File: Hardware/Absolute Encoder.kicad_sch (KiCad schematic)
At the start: 13 parts, among them J1 PISO_OUT, J2 PISO_IN, U1 74LS165

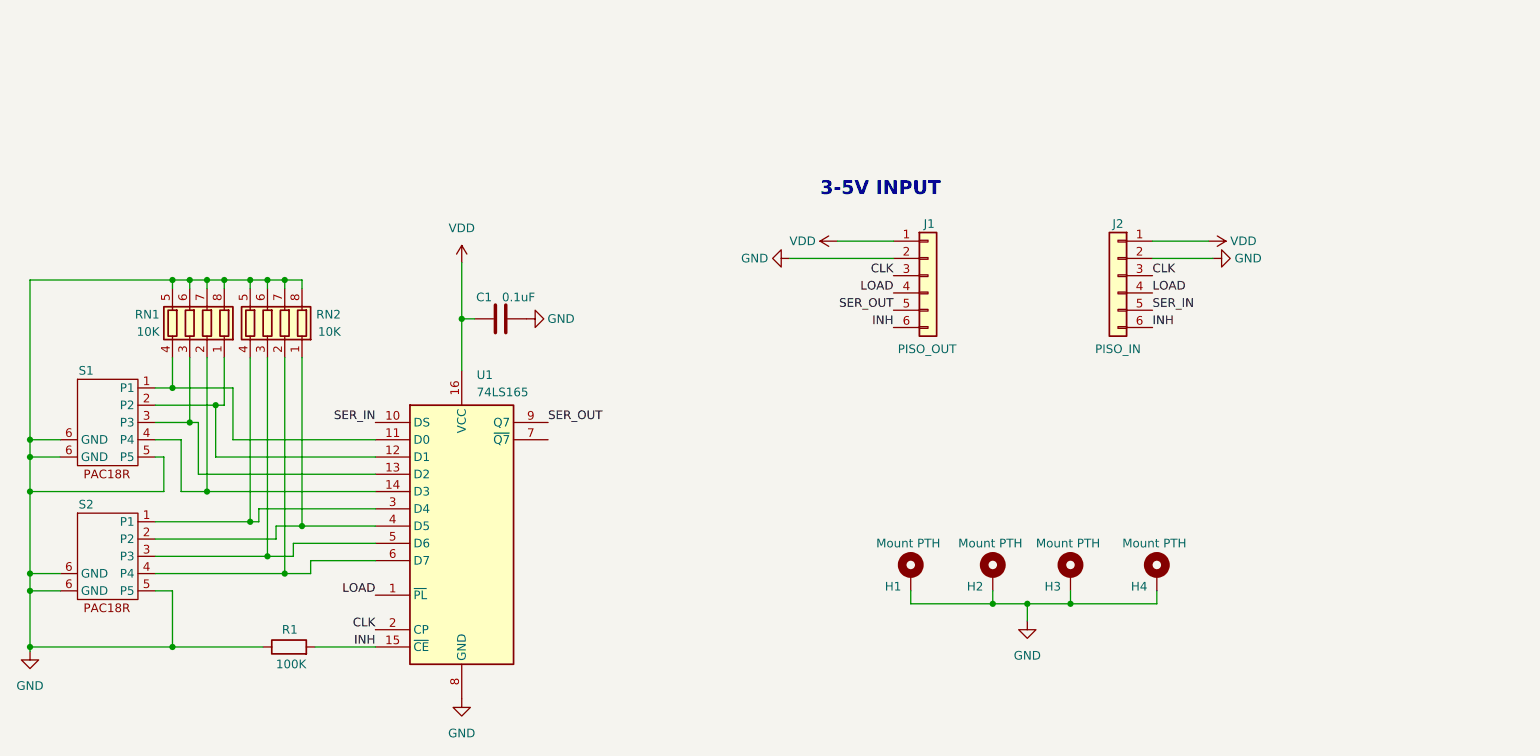
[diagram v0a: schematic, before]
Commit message: change R network for individual Rs
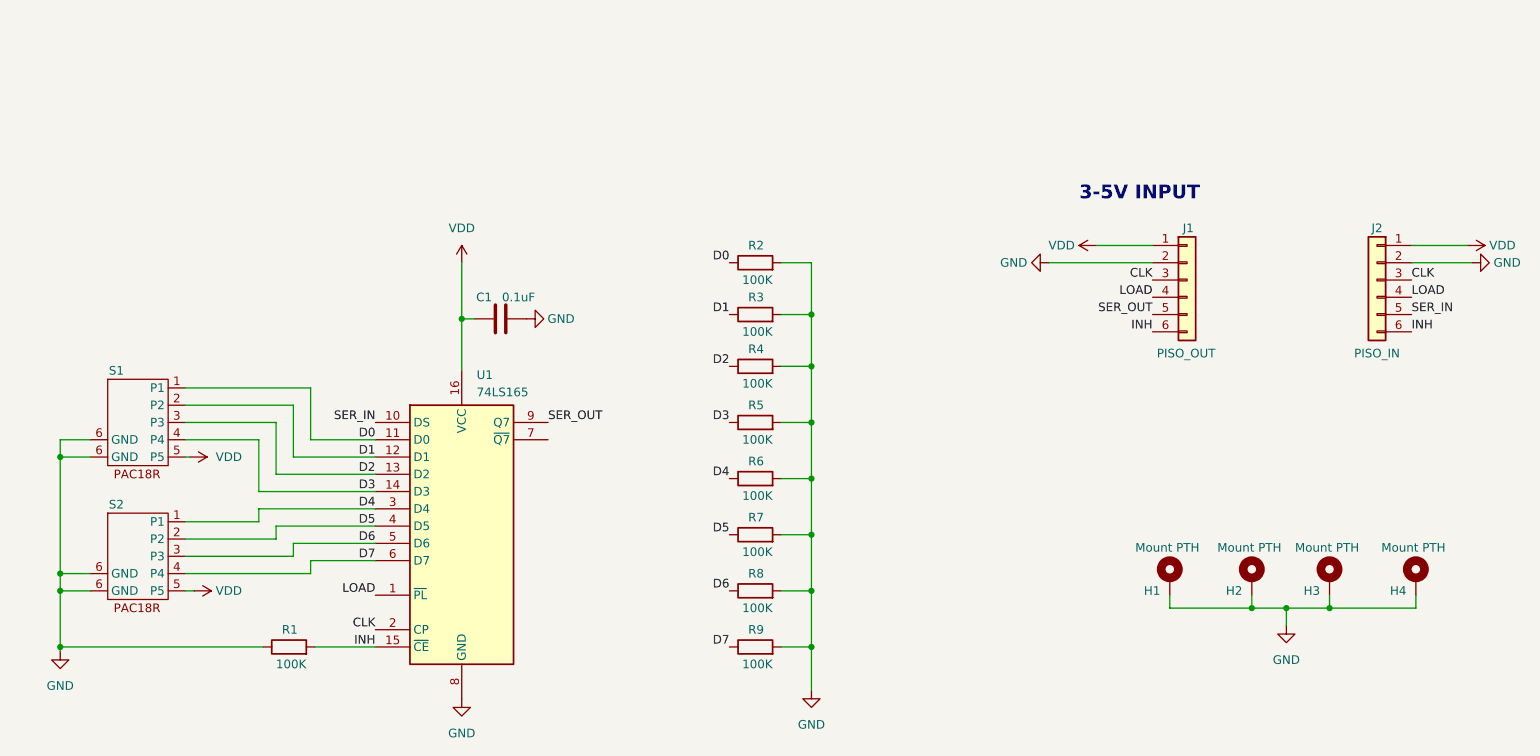
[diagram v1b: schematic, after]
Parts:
- removed RN1, RN2: 10K, Resistor_SMD:R_Array_Concave_4x0402, symbol Device:R_Pack04
- added R2, R3, R4, R5, R6, R7, R8, R9: 100K, Resistor_SMD:R_0402_1005Metric, symbol Device:R
- R1: footprint Resistor_SMD:R_0603_1608Metric -> Resistor_SMD:R_0402_1005Metric
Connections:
- net GND: now also R2.2, R3.2, R4.2, R5.2, R6.2, R7.2, R8.2, R9.2; no longer S1.5 (P5), S2.5 (P5)
- net VDD: now also S1.5 (P5), S2.5 (P5)
- net D4: now reaches S2.1 (P1), U1.3 (D4)
- net D4: now also R6.1
- net D5: now reaches S2.2 (P2), U1.4 (D5)
- net D5: now also R7.1
- net D6: now reaches S2.3 (P3), U1.5 (D6)
- net D6: now also R8.1
- net D7: now reaches S2.4 (P4), U1.6 (D7)
- net D7: now also R9.1
- net D0: now reaches S1.1 (P1), U1.11 (D0)
- net D0: now also R2.1
- net D1: now reaches S1.2 (P2), U1.12 (D1)
- net D1: now also R3.1
- net D2: now reaches S1.3 (P3), U1.13 (D2)
- net D2: now also R4.1
- net D3: now reaches S1.4 (P4), U1.14 (D3)
- net D3: now also R5.1
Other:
- moved on the sheet: H1, H2, H3, H4, J1, J2, S1, S2

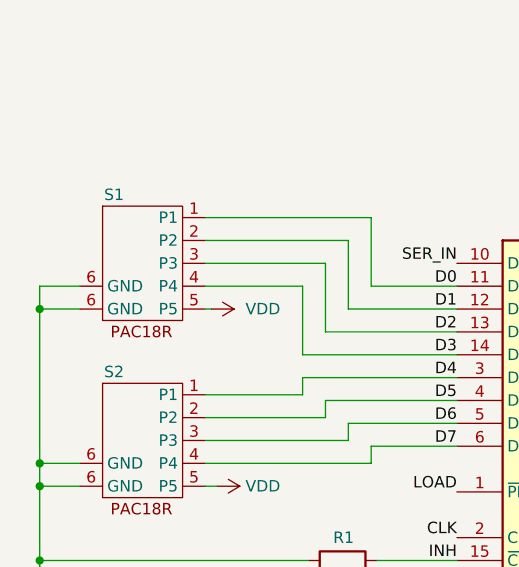
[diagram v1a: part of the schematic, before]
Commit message: Update Readme
add license
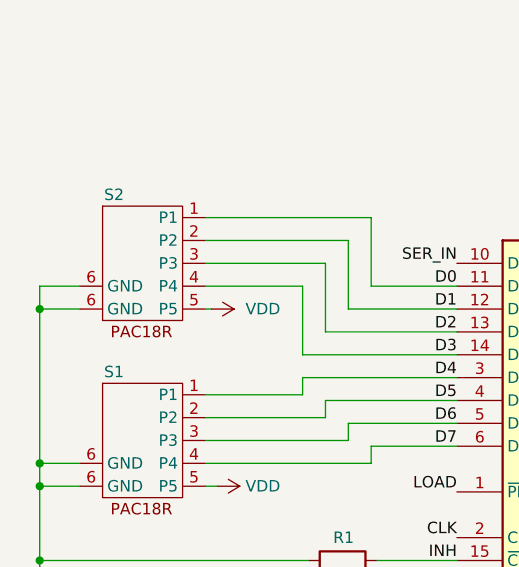
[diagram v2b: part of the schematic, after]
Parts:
- renumbered S2 to S1, S1 to S2
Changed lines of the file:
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@@
 		(on_board yes)
 		(dnp no)
-		(property "Reference" "S2"
+		(property "Reference" "S1"
 			(at 61.595 102.235 0)
 			(effects
@@
 			(project "Absolute Encoder"
 				(path "/e9a1f795-9b0b-4ff9-9b00-3d3b4875d365"
-					(reference "S2")
+					(reference "S1")
 					(unit 1)
 				)
@@
 		(on_board yes)
 		(dnp no)
-		(property "Reference" "S1"
+		(property "Reference" "S2"
 			(at 61.595 82.55 0)
 			(effects
@@
 			(project "Absolute Encoder"
 				(path "/e9a1f795-9b0b-4ff9-9b00-3d3b4875d365"
-					(reference "S1")
-					(unit 1)
-				)
+					(reference "S2")
+					(unit 1)
+				)

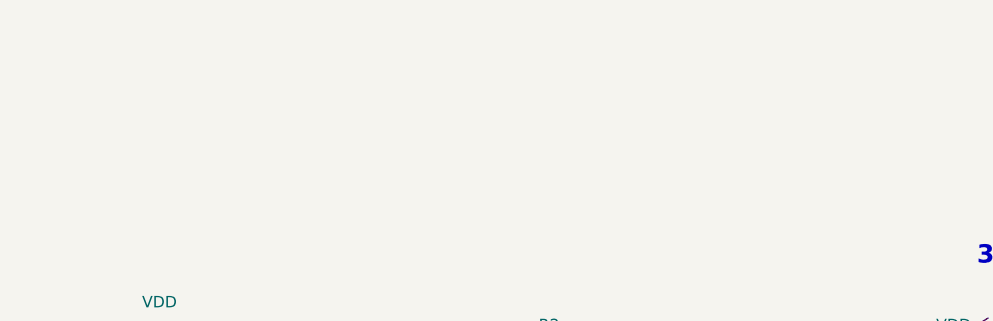
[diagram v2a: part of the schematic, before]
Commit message: Moved custom parts to local path
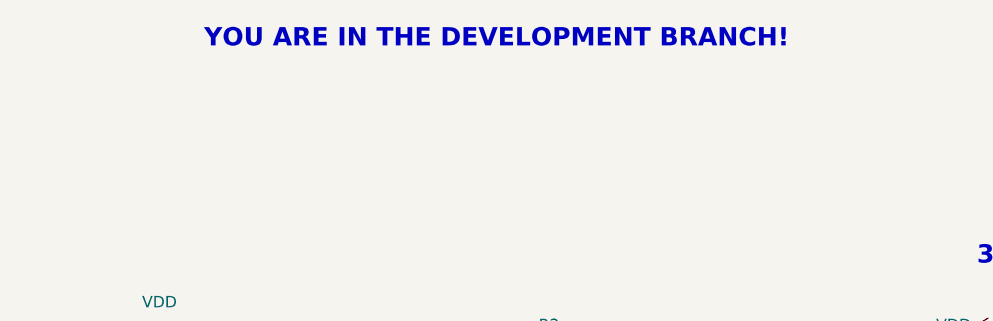
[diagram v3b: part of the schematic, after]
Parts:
- removed S1, S2: ~, Flywheel:PAC18R, symbol Flywheel_Library:PAC18R
- added S1, S2: ~, AbsoluteEncoder:PAC18R, symbol AbsoluteEncoder_Library:PAC18R
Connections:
- net D0: now also S2.1 (P1)
- net D1: now also S2.2 (P2)
- net D2: now also S2.3 (P3)
- net D3: now also S2.4 (P4)
- net D4: now also S1.1 (P1)
- net D5: now also S1.2 (P2)
- net D6: now also S1.3 (P3)
- net D7: now also S1.4 (P4)
- net GND: now also S1.6 (GND), S2.6 (GND)
- net VDD: now also S1.5 (P5), S2.5 (P5)
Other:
- note added: "YOU ARE IN THE DEVELOPMENT BRANCH!"
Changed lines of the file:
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@@
 		)
 	)
-	(text "3-5V INPUT"
-		(exclude_from_sim no)
-		(at 212.09 56.515 0)
+	(text "YOU ARE IN THE DEVELOPMENT BRANCH!"
+		(exclude_from_sim no)
+		(at 149.86 32.385 0)
 		(effects
 			(font
@@
 		)
 	)
+	(text "3-5V INPUT"
+		(exclude_from_sim no)
+		(at 212.09 56.515 0)
+		(effects
+			(font
+				(size 2.032 2.032)
+				(thickness 0.4064)
+				(bold yes)
+			)
+		)
+	)
 	(label "CLK"
 		(at 213.995 69.215 180)
@@
 				(path "/e9a1f795-9b0b-4ff9-9b00-3d3b4875d365"
 					(reference "#PWR09")
-					(unit 1)
-				)
-			)
-		)
-	)
-	(symbol
-		(lib_name "Flywheel_Library:PAC18R")
-		(lib_id "Flywheel_Library:PAC18R")
-		(at 64.135 109.855 0)
-		(unit 1)
-		(exclude_from_sim no)
-		(in_bom yes)
-		(on_board yes)
-		(dnp no)
-		(property "Reference" "S1"
-			(at 61.595 102.235 0)
-			(effects
-				(font
-					(size 1.27 1.27)
-				)
-			)
-		)
-		(property "Value" "~"
-			(at 64.77 102.235 0)
-			(effects
-				(font
-					(size 1.27 1.27)
-				)
-			)
-		)
-		(property "Footprint" "Flywheel:PAC18R"
-			(at 69.215 104.775 0)
-			(effects
-				(font
-					(size 1.27 1.27)
-				)
-				(hide yes)
-			)
-		)
-		(property "Datasheet" "https://www.mouser.com/datasheet/2/54/pac18r-2511013.pdf"
-			(at 69.215 104.775 0)
-			(effects
-				(font
-					(size 1.27 1.27)
-				)
-				(hide yes)
-			)
-		)
-		(property "Description" "Grey Code Encoder Switch"
-			(at 69.215 104.775 0)
-			(effects
-				(font
-					(size 1.27 1.27)
-				)
-				(hide yes)
-			)
-		)
-		(pin "3"
-		)
-		(pin "4"
-		)
-		(pin "5"
-		)
-		(pin "2"
-		)
-		(pin "1"
-		)
-		(pin "6"
-		)
-		(pin "6"
-		)
-		(instances
-			(project "Absolute Encoder"
-				(path "/e9a1f795-9b0b-4ff9-9b00-3d3b4875d365"
-					(reference "S1")
 					(unit 1)
 				)
@@
 	)
 	(symbol
+		(lib_name "AbsoluteEncoder_Library:PAC18R")
+		(lib_id "AbsoluteEncoder_Library:PAC18R")
+		(at 64.135 109.855 0)
+		(unit 1)
+		(exclude_from_sim no)
+		(in_bom yes)
+		(on_board yes)
+		(dnp no)
+		(property "Reference" "S1"
+			(at 61.595 102.235 0)
+			(effects
+				(font
+					(size 1.27 1.27)
+				)
+			)
+		)
+		(property "Value" "~"
+			(at 64.77 102.235 0)
+			(effects
+				(font
+					(size 1.27 1.27)
+				)
+			)
+		)
+		(property "Footprint" "AbsoluteEncoder:PAC18R"
+			(at 69.215 104.775 0)
+			(effects
+				(font
+					(size 1.27 1.27)
+				)
+				(hide yes)
+			)
+		)
+		(property "Datasheet" "https://www.mouser.com/datasheet/2/54/pac18r-2511013.pdf"
+			(at 69.215 104.775 0)
+			(effects
+				(font
+					(size 1.27 1.27)
+				)
+				(hide yes)
+			)
+		)
+		(property "Description" "Grey Code Encoder Switch"
+			(at 69.215 104.775 0)
+			(effects
+				(font
+					(size 1.27 1.27)
+				)
+				(hide yes)
+			)
+		)
+		(pin "1"
+		)
+		(pin "3"
+		)
+		(pin "2"
+		)
+		(pin "4"
+		)
+		(pin "5"
+		)
+		(pin "6"
+		)
+		(pin "6"
+		)
+		(instances
+			(project ""
+				(path "/e9a1f795-9b0b-4ff9-9b00-3d3b4875d365"
+					(reference "S1")
+					(unit 1)
+				)
+			)
+		)
+	)
+	(symbol
 		(lib_id "Device:R")
 		(at 155.575 74.295 90)
@@
 	)
 	(symbol
-		(lib_name "Flywheel_Library:PAC18R")
-		(lib_id "Flywheel_Library:PAC18R")
+		(lib_id "Device:R")
+		(at 155.575 106.68 90)
+		(unit 1)
+		(exclude_from_sim no)
+		(in_bom yes)
+		(on_board yes)
+		(dnp no)
+		(property "Reference" "R7"
+			(at 156.845 104.14 90)
+			(effects
+				(font
+					(size 1.27 1.27)
+				)
+				(justify left)
+			)
+		)
+		(property "Value" "100K"
+			(at 158.115 109.22 90)
+			(effects
+				(font
+					(size 1.27 1.27)
+				)
+				(justify left)
+			)
+		)
+		(property "Footprint" "Resistor_SMD:R_0402_1005Metric"
+			(at 155.575 108.458 90)
+			(effects
+				(font
+					(size 1.27 1.27)
+				)
+				(hide yes)
+			)
+		)
+		(property "Datasheet" "~"
+			(at 155.575 106.68 0)
+			(effects
+				(font
+					(size 1.27 1.27)
+				)
+				(hide yes)
+			)
+		)
+		(property "Description" "Resistor"
+			(at 155.575 106.68 0)
+			(effects
+				(font
+					(size 1.27 1.27)
+				)
+				(hide yes)
+			)
+		)
+		(pin "1"
+		)
+		(pin "2"
+		)
+		(instances
+			(project "Absolute Encoder"
+				(path "/e9a1f795-9b0b-4ff9-9b00-3d3b4875d365"
+					(reference "R7")
+					(unit 1)
+				)
+			)
+		)
+	)
+	(symbol
+		(lib_name "AbsoluteEncoder_Library:PAC18R")
+		(lib_id "AbsoluteEncoder_Library:PAC18R")
 		(at 64.135 90.17 0)
 		(unit 1)
@@
 			)
 		)
-		(property "Footprint" "Flywheel:PAC18R"
+		(property "Footprint" "AbsoluteEncoder:PAC18R"
 			(at 69.215 85.09 0)
 			(effects
@@
 			)
 		)
+		(pin "1"
+		)
 		(pin "3"
 		)
+		(pin "2"
+		)
 		(pin "4"
 		)
 		(pin "5"
 		)
-		(pin "2"
-		)
-		(pin "1"
-		)
 		(pin "6"
 		)
@@
 					(unit 1)
 				)
-			)
-		)
-	)
-	(symbol
-		(lib_id "Device:R")
-		(at 155.575 106.68 90)
-		(unit 1)
-		(exclude_from_sim no)
-		(in_bom yes)
-		(on_board yes)
-		(dnp no)
-		(property "Reference" "R7"
-			(at 156.845 104.14 90)
-			(effects
-				(font
-					(size 1.27 1.27)
-				)
-				(justify left)
-			)
-		)
-		(property "Value" "100K"
-			(at 158.115 109.22 90)
-			(effects
-				(font
-					(size 1.27 1.27)
-				)
-				(justify left)
-			)
-		)
-		(property "Footprint" "Resistor_SMD:R_0402_1005Metric"
-			(at 155.575 108.458 90)
-			(effects
-				(font
-					(size 1.27 1.27)
-				)
-				(hide yes)
-			)
-		)
-		(property "Datasheet" "~"
-			(at 155.575 106.68 0)
-			(effects
-				(font
-					(size 1.27 1.27)
-				)
-				(hide yes)
-			)
-		)
-		(property "Description" "Resistor"
-			(at 155.575 106.68 0)
-			(effects
-				(font
-					(size 1.27 1.27)
-				)
-				(hide yes)
-			)
-		)
-		(pin "1"
-		)
-		(pin "2"
-		)
-		(instances
-			(project "Absolute Encoder"
-				(path "/e9a1f795-9b0b-4ff9-9b00-3d3b4875d365"
-					(reference "R7")
-					(unit 1)
-				)

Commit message: removed erroneous text
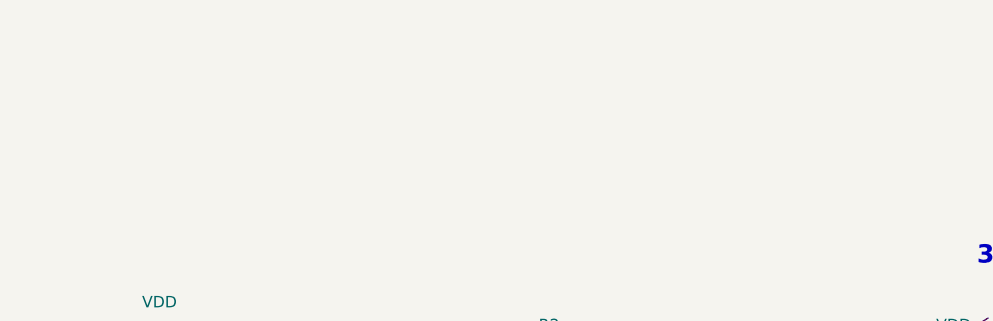
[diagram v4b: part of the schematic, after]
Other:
- note removed: "YOU ARE IN THE DEVELOPMENT BRANCH!"
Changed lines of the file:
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@@
 		)
 	)
-	(text "YOU ARE IN THE DEVELOPMENT BRANCH!"
+	(text "3-5V INPUT"
 		(exclude_from_sim no)
-		(at 149.86 32.385 0)
+		(at 212.09 56.515 0)
 		(effects
 			(font
@@
 		)
 	)
-	(text "3-5V INPUT"
-		(exclude_from_sim no)
-		(at 212.09 56.515 0)
-		(effects
-			(font
-				(size 2.032 2.032)
-				(thickness 0.4064)
-				(bold yes)
-			)
-		)
-	)
 	(label "CLK"
 		(at 213.995 69.215 180)
@@
 	)
 	(symbol
-		(lib_name "AbsoluteEncoder_Library:PAC18R")
 		(lib_id "AbsoluteEncoder_Library:PAC18R")
 		(at 64.135 109.855 0)
@@
 	)
 	(symbol
-		(lib_name "AbsoluteEncoder_Library:PAC18R")
 		(lib_id "AbsoluteEncoder_Library:PAC18R")
 		(at 64.135 90.17 0)
